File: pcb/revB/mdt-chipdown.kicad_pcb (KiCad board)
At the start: 4 copper layers, 94 x 79.6 mm, 134 parts, among them J1 BI, J2 BI, J3 SPDIF OUT, J4 Micro_SD_Card, J5 Micro_SD_Card, Q1 DMG2305UX, SW1 ON_OFF, SW2 PROGRAM, U1 TPD3S014, U10 TLV75733PDBV, U2 AMS1117-3.3, U3 ILI9341 3.2" capacitive touch, U4 PCM5102A, U5 APS6404L-3SQR, U6 APS6404L-3SQR, U7 MKL02Z32VFG4, U8 GD25Q64ESIGR, U9 MIMXRT1062DVJ6B, Y1 24MHz, Y2 32768

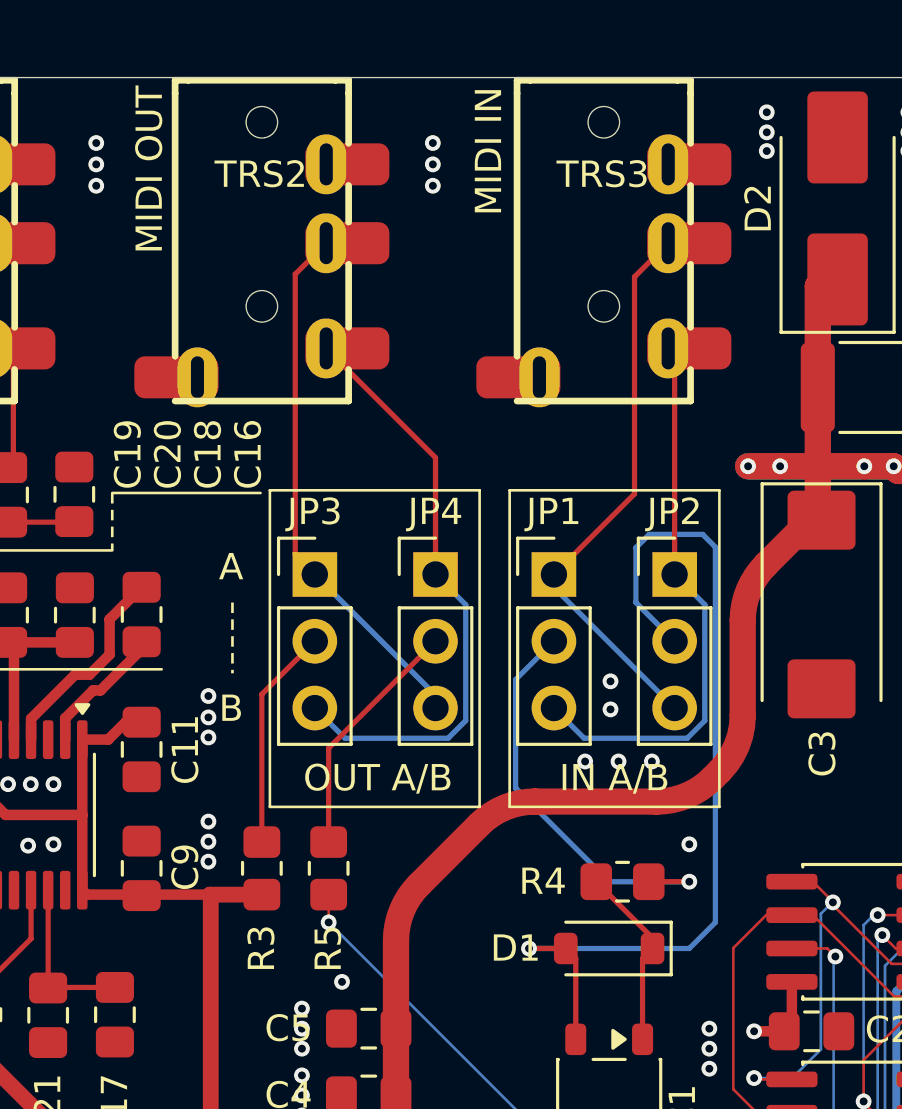
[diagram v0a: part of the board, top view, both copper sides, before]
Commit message: updated revB with solder jumpers
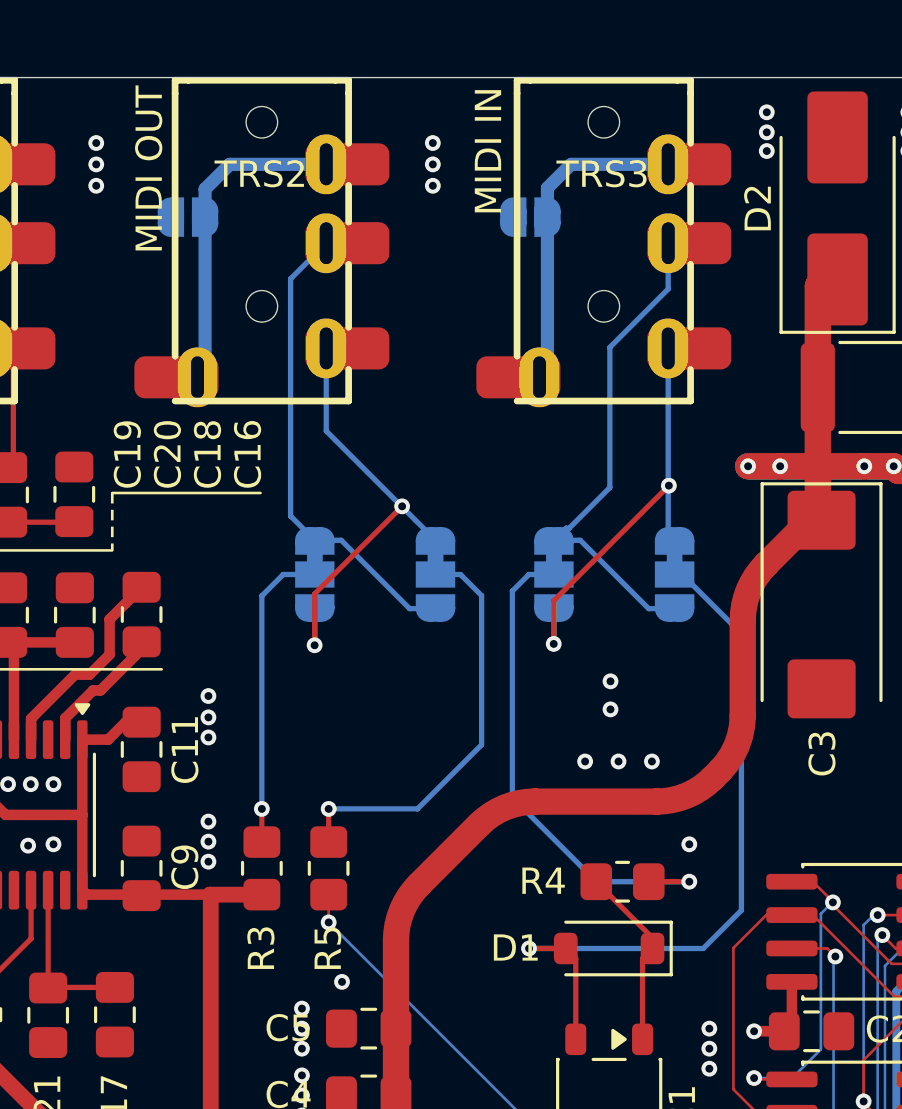
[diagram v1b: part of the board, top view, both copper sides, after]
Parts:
- added JP5: Jumper_2_Open, Jumper:SolderJumper-2_P1.3mm_Open_RoundedPad1.0x1.5mm, B.Cu at (70.9, 39.2)
- added JP6: Jumper_2_Open, Jumper:SolderJumper-2_P1.3mm_Open_RoundedPad1.0x1.5mm, B.Cu at (83.9, 39.2)
- JP1, JP2, JP3, JP4: footprint Connector_PinHeader_2.54mm:PinHeader_1x03_P2.54mm_Vertical -> Jumper:SolderJumper-3_P1.3mm_Bridged12_RoundedPad1.0x1.5mm; moved to B.Cu
- turned JP1 to -90 degrees
- turned JP2 to -90 degrees
- turned JP3 to -90 degrees
- turned JP4 to -90 degrees
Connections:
- TRS2 pad R2: GND -> Net-(JP5-A)
- TRS2 pad S: GND -> Net-(JP5-A)
- TRS3 pad R2: GND -> Net-(JP6-A)
- TRS3 pad S: GND -> Net-(JP6-A)
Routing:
- net Net-(JP6-A): track 0.00 -> 12.3 mm
- net Net-(JP5-A): track 0.00 -> 12.3 mm
- net Net-(D1-A): track 34.4 -> 27.7 mm
- net Net-(JP4-C): track 9.32 -> 15.8 mm, vias 0 -> 1
- net Net-(JP3-B): track 22.8 -> 17.1 mm, vias 0 -> 2
- net Net-(JP1-B): track 21.2 -> 16.6 mm, vias 0 -> 2
- net Net-(JP1-C): track 15.8 -> 19.3 mm
- net Net-(JP3-C): track 8.47 -> 11.7 mm, vias 0 -> 1
- net Net-(JP1-A): track 21.4 -> 18.8 mm
- net Net-(JP3-A): track 20.4 -> 17.9 mm
